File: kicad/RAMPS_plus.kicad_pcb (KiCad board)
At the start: 2 copper layers, 120.7 x 66 mm, 135 parts, among them CON1 CON10, CON10 Stepstick_Left_Connector, CON11 Stepstick_Right_Connector, CON12 Stepstick_Left_Connector, CON13 Stepstick_Right_Connector, CON14 Stepstick_Left_Connector, CON15 Stepstick_Right_Connector, CON16 CON14x2, CON17 Stepstick_Left_Connector, CON18 Stepstick_Right_Connector, CON19 Stepstick_Left_Connector, CON2 CON8, CON20 Stepstick_Right_Connector, CON21 Panel1, CON22 Panel2, CON23 PS-ON, CON24 CON6, CON25 FAN, CON26 Chamber, CON27 BED, CON28 BED_Th, CON3 CON8, CON4 CON8, CON5 AUX, CON6 CON8, CON7 CON8, CON8 CON18x2, CON9 Carriage, Q1 IRLR2905ZPBF, Q2 IRLR2905ZPBF, Q3 FDC6401N, Q4 FDC6401N, Q5 IRLR2905ZPBF, Q6 FDC6401N, Q7 FDC6401N, Q8 FDC6401N, Q9 FDC6401N, SW1 RESET, U1 CD4504BPW, U2 SN74HCT245PW

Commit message: Route.
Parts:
- C11, C12, R9, U1: moved to F.Cu
- moved U1 33.6 mm to (47.0, 48.3), turned to 270 degrees
- moved C11 32.9 mm to (51.4, 45.7), turned to 90 degrees
- moved C12 32.3 mm to (51.4, 50.2), turned to 270 degrees
- moved R21 15.4 mm to (40.6, 57.1), turned to 90 degrees
- moved D12 9.91 mm to (38.7, 41.3), turned to 270 degrees
- moved R29 5.77 mm to (42.5, 45.6), turned to 90 degrees
- moved D15 5.43 mm to (41.3, 41.3), turned to 270 degrees
- moved R22 5.43 mm to (78.1, 36.8), turned to 0 degrees
- moved R18 4.78 mm to (40.1, 45.6), turned to 90 degrees
- moved R9 3.81 mm to (76.2, 32.4), turned to 270 degrees
- moved D1 2.40 mm to (48.0, 57.6), turned to 0 degrees
- moved Q7 1.42 mm to (45.1, 41.3)
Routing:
- net Vbed: track 10.8 -> 33.3 mm
- net Net-(D12-Pad1): track 2.66 -> 0.00 mm
- net GND: track 116.0 -> 115.2 mm

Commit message: Routing
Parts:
- moved C2 0.69 mm to (44.4, 76.5)
- moved U2 0.18 mm to (140.4, 49.4)
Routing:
- net +5V: track 8.94 -> 197.3 mm, vias 0 -> 6
- net Vheat: track 16.4 -> 70.6 mm, vias 0 -> 3
- net D8: track 0.00 -> 46.8 mm
- net GND: track 115.2 -> 159.0 mm, vias 14 -> 21
- net D10: track 0.00 -> 43.3 mm, vias 0 -> 1
- net A15: track 48.3 -> 6.39 mm
- net D9: track 0.00 -> 41.6 mm, vias 0 -> 1
- net /Carriage/heater1: track 0.00 -> 34.3 mm, vias 0 -> 1
- net D11: track 0.00 -> 28.2 mm
- net A8: track 2.60 -> 30.1 mm, vias 0 -> 1
- net A11: track 42.3 -> 14.8 mm
- net D13: track 0.00 -> 27.4 mm, vias 0 -> 2
- net /Carriage/heater2: track 0.00 -> 26.9 mm, vias 0 -> 1
- net A10: track 37.3 -> 10.6 mm
- net A9: track 39.1 -> 12.5 mm
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
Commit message: Swap pins
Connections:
- C15 pad 1: D14 -> D2
- C16 pad 1: D18 -> D14
- C17 pad 1: D15 -> D25
- C18 pad 1: D19 -> D3
- C6 pad 1: D2 -> D21
- C8 pad 1: D3 -> D20
- CON10 pad 1: D38 -> A7
- CON10 pad 7: A0 -> A8
- CON10 pad 8: A1 -> A12
- CON12 pad 1: D24 -> D46
- CON12 pad 7: D26 -> D38
- CON12 pad 8: D28 -> D36
- CON14 pad 1: D30 -> D34
- CON14 pad 7: D36 -> D30
- CON14 pad 8: D34 -> D28
- CON17 pad 1: A8 -> A4
- CON17 pad 7: D46 -> A5
- CON17 pad 8: D48 -> A6
- CON19 pad 1: A2 -> A0
- CON19 pad 7: A6 -> A1
- CON19 pad 8: A7 -> A2
- CON3 pad 4: A3 -> (no net)
- CON3 pad 6: (no net) -> A5
- CON6 pad 5: (no net) -> A12
- CON7 pad 2: D15 -> (no net)
- CON7 pad 5: D18 -> (no net)
- CON7 pad 6: D19 -> (no net)
- CON7 pad 7: (no net) -> D20
- CON7 pad 8: (no net) -> D21
- CON8 pad 29: D48 -> (no net)
- Q9 pad 1: A4 -> D26
- Q9 pad 3: A3 -> D24
- R1 pad 2: D38 -> A7
- R12 pad 1: D2 -> D21
- R14 pad 2: D30 -> D34
- R15 pad 1: D3 -> D20
- R17 pad 2: A8 -> A4
- R23 pad 2: A2 -> A0
- R24 pad 1: D14 -> D2
- R25 pad 1: D18 -> D14
- R26 pad 1: D15 -> D25
- R27 pad 1: D19 -> D3
- R7 pad 2: D24 -> D46
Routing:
- net D24: track 76.5 -> 2.56 mm, vias 3 -> 0
- net D26: track 45.1 -> 2.49 mm, vias 2 -> 0
- net D38: track 3.12 -> 42.6 mm, vias 0 -> 2
- net A5: track 0.00 -> 38.4 mm
- net D36: track 14.4 -> 51.4 mm, vias 0 -> 2
- net D48: track 36.5 -> 0.00 mm
- net A12: track 0.00 -> 35.5 mm, vias 0 -> 1
- net D46: track 40.9 -> 76.4 mm, vias 0 -> 3
- net A6: track 26.8 -> 60.8 mm
- net A1: track 43.0 -> 9.99 mm, vias 1 -> 0
- net A8: track 30.1 -> 56.6 mm
- net D28: track 40.8 -> 15.0 mm, vias 2 -> 0
- net D30: track 34.7 -> 10.9 mm
- net A7: track 27.9 -> 5.59 mm
- net D34: track 12.1 -> 24.7 mm
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
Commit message: Route
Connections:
- CON12 pad 1: D46 -> D28
- CON12 pad 7: D38 -> D30
- CON12 pad 8: D36 -> D34
- CON14 pad 1: D34 -> D36
- CON14 pad 7: D30 -> D38
- CON14 pad 8: D28 -> D46
- R14 pad 2: D34 -> D36
- R7 pad 2: D46 -> D28
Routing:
- net D46: track 76.4 -> 11.4 mm, vias 3 -> 0
- net A6: track 60.8 -> 4.84 mm
- net D28: track 15.0 -> 70.3 mm, vias 0 -> 3
- net A8: track 56.6 -> 15.5 mm, vias 1 -> 0
- net A5: track 38.4 -> 4.84 mm
- net D30: track 10.9 -> 42.3 mm, vias 1 -> 2
- net D38: track 42.6 -> 12.0 mm, vias 2 -> 0
- net A12: track 35.5 -> 8.28 mm, vias 1 -> 0
- net A2: track 27.9 -> 11.7 mm
- net D34: track 24.7 -> 39.8 mm, vias 0 -> 2
- net D36: track 51.4 -> 36.9 mm, vias 2 -> 1
- net IOREF: track 120.5 -> 107.7 mm
- net A0: track 39.2 -> 31.7 mm
- net A11: track 14.8 -> 10.8 mm
- net A7: track 5.59 -> 9.41 mm
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
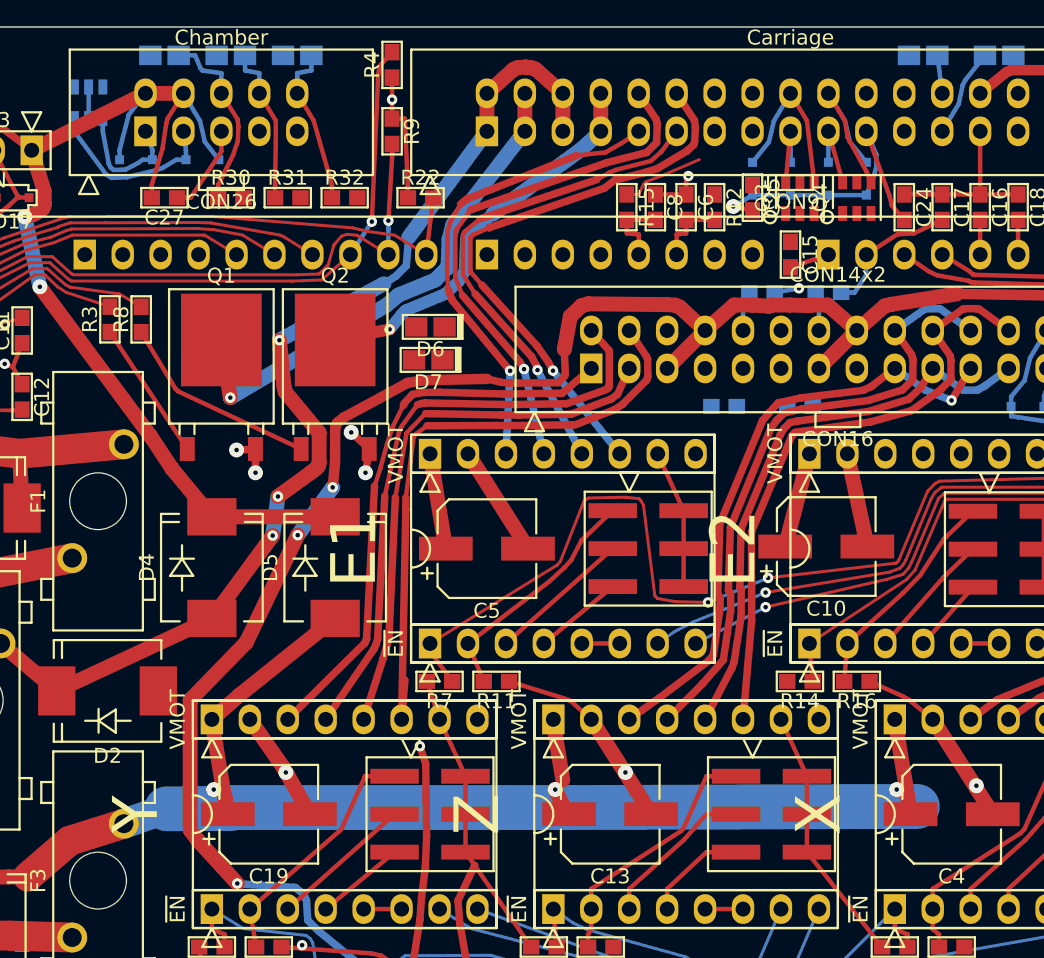
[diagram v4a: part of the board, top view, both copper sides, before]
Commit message: Exchange stepstick connections.
Simplify layout
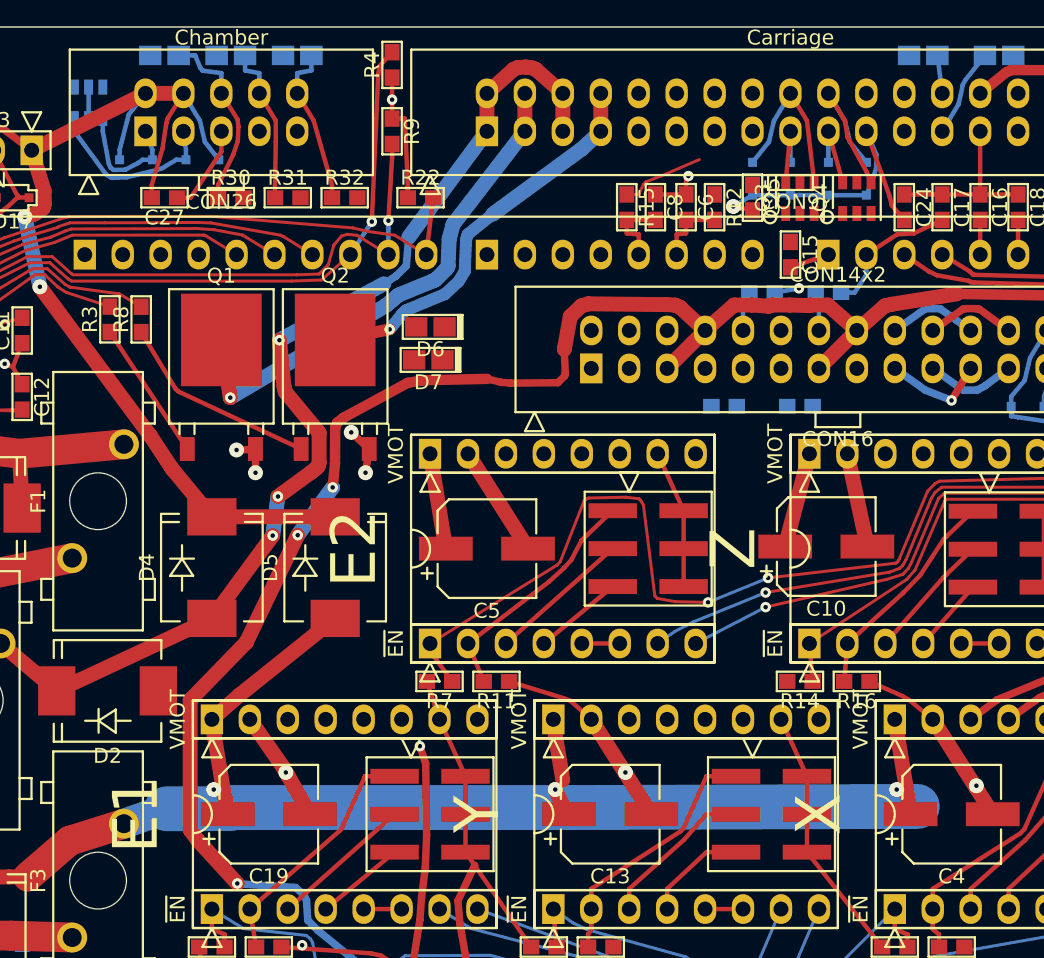
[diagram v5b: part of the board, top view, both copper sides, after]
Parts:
- MECH3: value E1 -> E2
- MECH4: value E2 -> Z
- MECH5: value Z -> Y
- MECH6: value Y -> E1
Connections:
- CON13 pad 3: /Carriage/E1MotorA -> /Carriage/E2MotorA
- CON13 pad 4: /Carriage/E1MotorB -> /Carriage/E2MotorB
- CON13 pad 5: /Carriage/E1MotorC -> /Carriage/E2MotorC
- CON13 pad 6: /Carriage/E1MotorD -> /Carriage/E2MotorD
- CON15 pad 3: /Carriage/E2MotorA -> /YZ axis/ZmotorA
- CON15 pad 4: /Carriage/E2MotorB -> /YZ axis/ZmotorB
- CON15 pad 5: /Carriage/E2MotorC -> /YZ axis/ZmotorC
- CON15 pad 6: /Carriage/E2MotorD -> /YZ axis/ZmotorD
- CON18 pad 3: /YZ axis/ZmotorA -> /YZ axis/YmotorA
- CON18 pad 4: /YZ axis/ZmotorB -> /YZ axis/YmotorB
- CON18 pad 5: /YZ axis/ZmotorC -> /YZ axis/YmotorC
- CON18 pad 6: /YZ axis/ZmotorD -> /YZ axis/YmotorD
- CON20 pad 3: /YZ axis/YmotorA -> /Carriage/E1MotorA
- CON20 pad 4: /YZ axis/YmotorB -> /Carriage/E1MotorB
- CON20 pad 5: /YZ axis/YmotorC -> /Carriage/E1MotorC
- CON20 pad 6: /YZ axis/YmotorD -> /Carriage/E1MotorD
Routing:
- net /YZ axis/YmotorD: track 42.1 -> 0.00 mm
- net /YZ axis/YmotorB: track 39.9 -> 0.00 mm
- net /Carriage/E1MotorD: track 38.2 -> 0.00 mm, vias 1 -> 0
- net /YZ axis/YmotorA: track 37.1 -> 0.00 mm
- net /YZ axis/YmotorC: track 36.4 -> 0.00 mm
- net /YZ axis/ZmotorB: track 41.7 -> 6.01 mm
- net /Carriage/E1MotorB: track 35.4 -> 0.00 mm, vias 1 -> 0
- net /YZ axis/ZmotorD: track 40.8 -> 6.00 mm
- net /Carriage/E1MotorC: track 33.5 -> 0.00 mm, vias 1 -> 0
- net /YZ axis/ZmotorA: track 40.3 -> 6.89 mm
- net /YZ axis/ZmotorC: track 37.9 -> 6.00 mm
- net /Carriage/E1MotorA: track 31.6 -> 0.00 mm, vias 1 -> 0

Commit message: Route
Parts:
- C6, C8, R12, R15: moved to B.Cu
- moved SW1 71.1 mm to (61.2, 83.3), turned to 270 degrees
- moved R15 34.4 mm to (125.4, 29.4)
- moved C8 31.9 mm to (125.4, 33.0), turned to 90 degrees
- moved C6 31.8 mm to (127.4, 33.0), turned to 90 degrees
- moved R12 30.7 mm to (127.4, 29.4)
- moved D5 2.52 mm to (70.0, 60.9)
- moved D4 1.86 mm to (62.4, 60.9)
- moved D1 1.85 mm to (46.4, 56.7)
- moved C10 1.77 mm to (107.0, 60.3)
- moved R21 1.68 mm to (39.5, 55.9)
- moved F1 1.24 mm to (55.3, 56.8)
- moved JP3 0.72 mm to (118.2, 60.5)
- moved C12 0.37 mm to (51.1, 50.1)
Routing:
- net /Carriage/E1MotorD: track 0.00 -> 55.9 mm
- net /Carriage/E1MotorB: track 0.00 -> 55.5 mm
- net /Carriage/E1MotorA: track 0.00 -> 52.7 mm
- net /Carriage/E1MotorC: track 0.00 -> 52.4 mm
- net +12V: track 130.7 -> 182.1 mm, vias 3 -> 6
- net Vmot: track 113.4 -> 155.4 mm, vias 3 -> 8
- net /YZ axis/YmotorB: track 0.00 -> 33.2 mm
- net /Carriage/E2MotorB: track 0.00 -> 32.2 mm
- net /Carriage/E2MotorD: track 0.00 -> 32.0 mm
- net /YZ axis/YmotorA: track 0.00 -> 31.5 mm
- net /YZ axis/YmotorD: track 0.00 -> 31.0 mm
- net /Carriage/E2MotorA: track 0.00 -> 30.3 mm
- net /YZ axis/YmotorC: track 0.00 -> 28.7 mm
- net /Carriage/E2MotorC: track 0.00 -> 28.4 mm
- net +5V: track 197.3 -> 178.6 mm, vias 6 -> 4
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
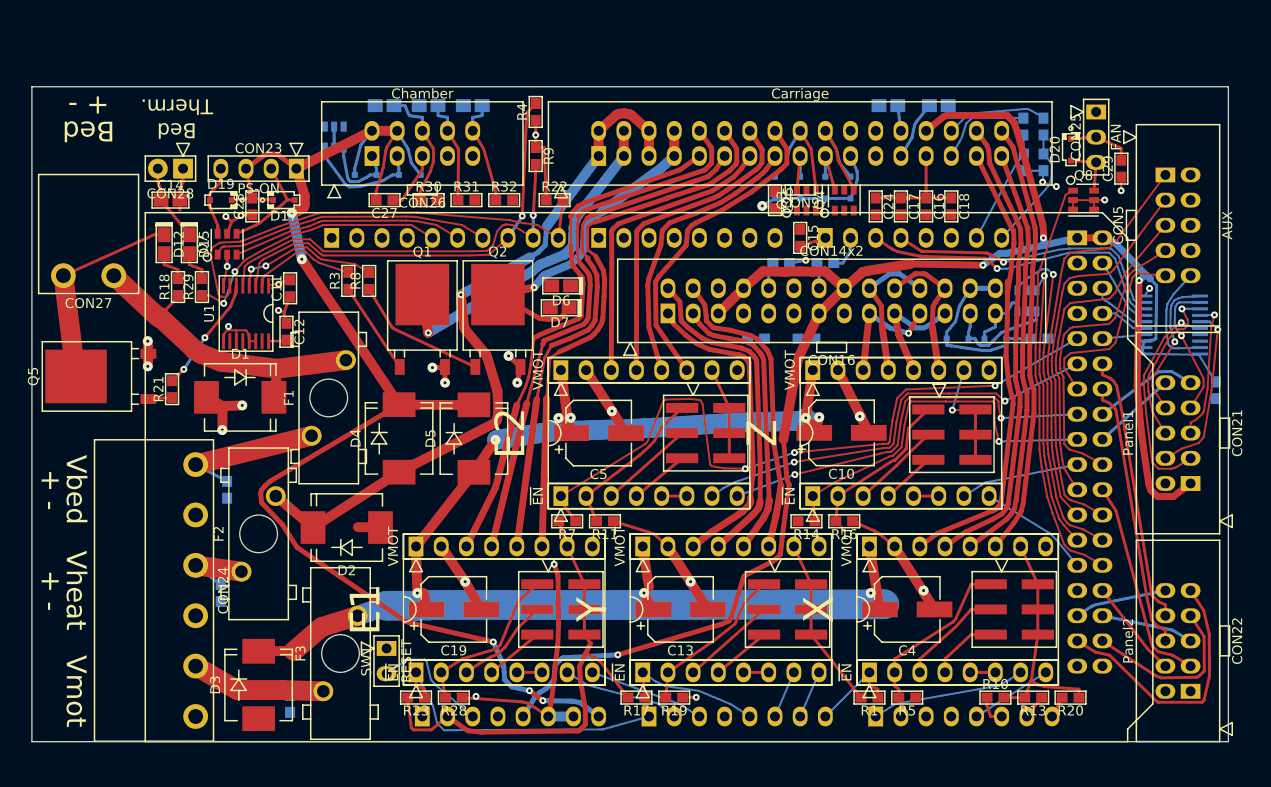
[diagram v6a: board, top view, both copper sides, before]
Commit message: Pin swap. Route.
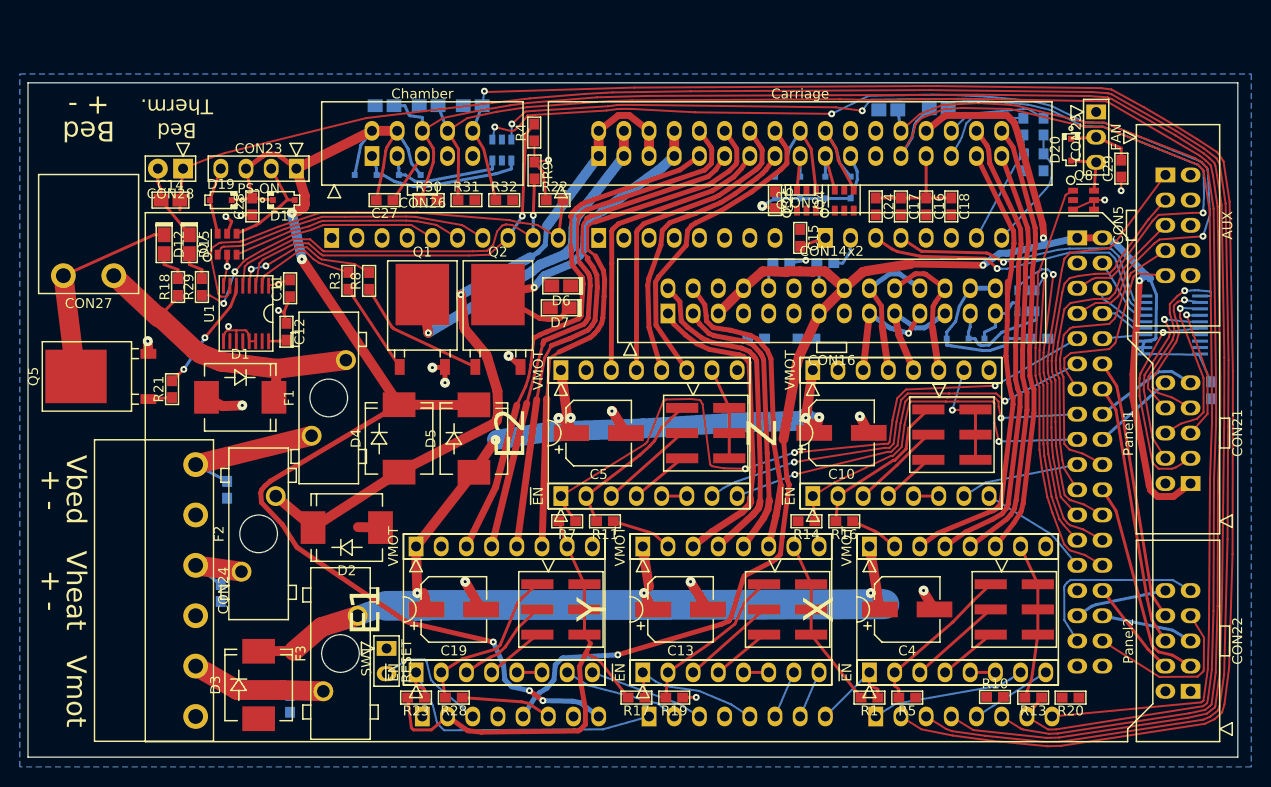
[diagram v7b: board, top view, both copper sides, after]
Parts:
- moved Q9 17.0 mm to (72.8, 31.8)
- moved R4 2.08 mm to (76.1, 30.0)
- moved R9 1.46 mm to (76.1, 33.8)
- moved C20 0.48 mm to (144.3, 56.0)
- moved C9 0.43 mm to (111.8, 27.7)
- moved C7 0.32 mm to (116.8, 27.6)
- moved R10 0.08 mm to (122.5, 86.9)
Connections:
- C14 pad 1: A15 -> A10
- C21 pad 1: A9 -> A11
- C22 pad 1: A10 -> A13
- C23 pad 1: A11 -> A9
- C7 pad 1: A13 -> A15
- CON26 pad 10: A11 -> A9
- CON26 pad 6: A9 -> A11
- CON26 pad 8: A10 -> A13
- CON28 pad 1: A15 -> A10
- CON9 pad 25: A13 -> A15
- R10 pad 2: A13 -> A15
- R20 pad 1: A15 -> A10
- R30 pad 2: A9 -> A11
- R31 pad 2: A10 -> A13
- R32 pad 2: A11 -> A9
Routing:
- net A10: track 10.6 -> 197.3 mm
- net A11: track 10.8 -> 177.1 mm
- net A9: track 12.5 -> 177.5 mm, vias 0 -> 1
- net A13: track 8.99 -> 165.7 mm
- net A14: track 4.98 -> 110.4 mm
- net A15: track 6.39 -> 108.8 mm
- net D26: track 0.00 -> 99.2 mm, vias 0 -> 3
- net D24: track 0.00 -> 94.3 mm, vias 0 -> 3
- net GND: track 172.8 -> 101.6 mm, vias 27 -> 19
- net /Power/Chamber-heater: track 8.37 -> 16.9 mm
- net IOREF: track 113.9 -> 106.0 mm
- net SCK: track 26.7 -> 19.2 mm
- net /Panel/LCD_EN: track 14.7 -> 18.1 mm
- net /Power/PS-FAN: track 9.60 -> 6.92 mm
- net /Panel/LCD_RS: track 14.0 -> 16.3 mm
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- added copper zone on B.Cu, net GND
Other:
- board size 120.7 x 66 mm -> 122 x 68 mm

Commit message: Add AGND. Route.
close #27
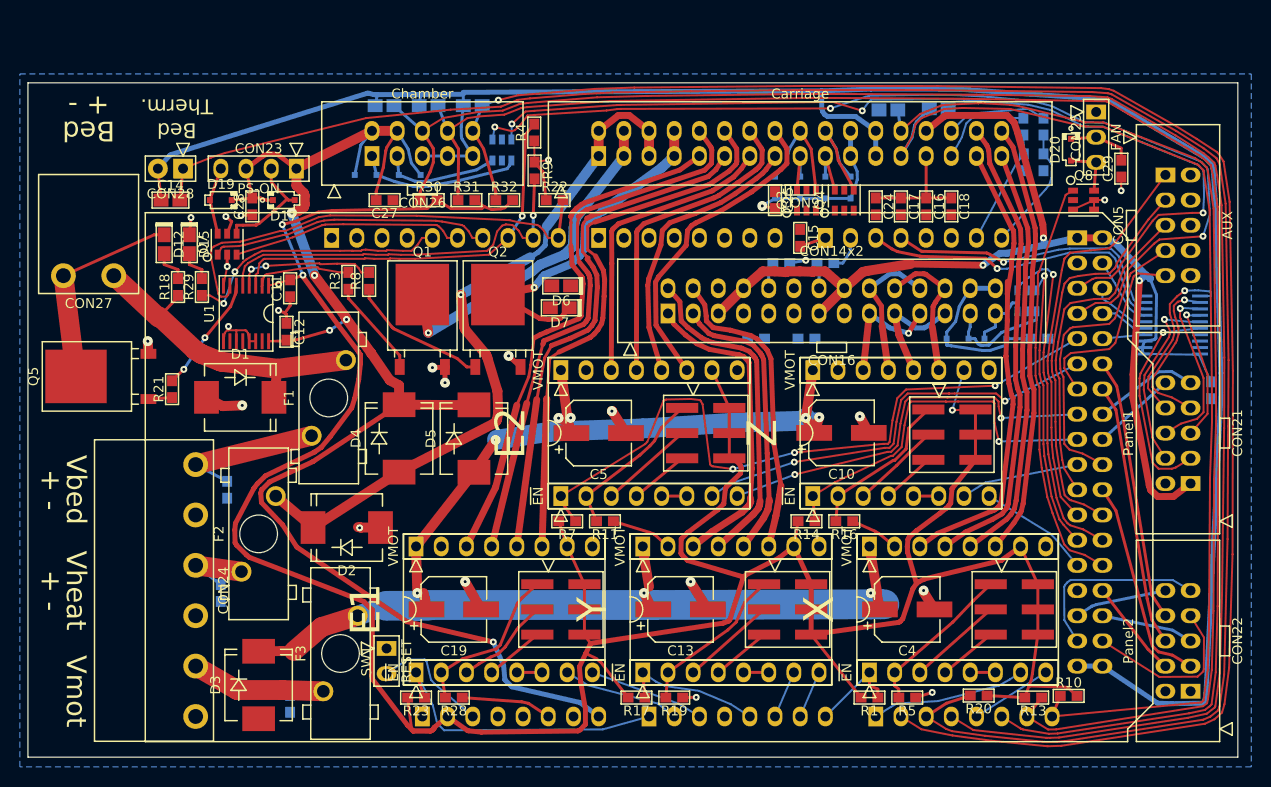
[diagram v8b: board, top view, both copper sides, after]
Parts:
- moved R20 9.26 mm to (120.9, 86.8)
- moved R10 7.43 mm to (129.9, 86.8)
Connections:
- C14 pad 2: GND -> AGND
- C21 pad 2: GND -> AGND
- C22 pad 2: GND -> AGND
- C23 pad 2: GND -> AGND
- C7 pad 2: GND -> AGND
- C9 pad 2: GND -> AGND
- CON2 pad 5: +5V -> (no net)
- CON26 pad 5: GND -> AGND
- CON26 pad 7: GND -> AGND
- CON26 pad 9: GND -> AGND
- CON28 pad 2: GND -> AGND
- CON8 pad 35: GND -> AGND
- CON8 pad 36: GND -> AGND
- CON9 pad 23: GND -> AGND
- CON9 pad 24: GND -> AGND
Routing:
- net AGND: track 0.00 -> 206.0 mm
- net IOREF: track 106.0 -> 300.7 mm, vias 1 -> 3
- net +5V: track 178.3 -> 119.5 mm, vias 4 -> 3
- net +12V: track 182.1 -> 191.9 mm
- net GND: track 101.6 -> 92.2 mm, vias 19 -> 22
- net A10: track 197.3 -> 201.4 mm
- net A15: track 108.8 -> 111.1 mm
- net Net-(R3-Pad1): track 11.1 -> 9.94 mm
- net A9: track 177.5 -> 176.4 mm
- net A11: track 177.1 -> 176.2 mm
- net /Power/PS-ON: track 10.6 -> 11.5 mm
- net Net-(R8-Pad1): track 14.8 -> 14.1 mm
- net D10: track 41.2 -> 40.5 mm
- net /Power/Chamber-fan: track 12.5 -> 11.9 mm
